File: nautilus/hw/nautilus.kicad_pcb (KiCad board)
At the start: 4 copper layers, 54.8 x 54 mm, 100 parts, among them IC1 DRV8353SRTAR, IC2 STM32G474CEU6, IC3 MAX15062AATA+T, J1 XT30XT30PW_MALE, J2 Conn_01x02_Pin, J3 Conn_01x02_Pin, U2 CSD88599Q5DCT, U3 CSD88599Q5DCT, U4 AS5147, U5 CSD88599Q5DCT

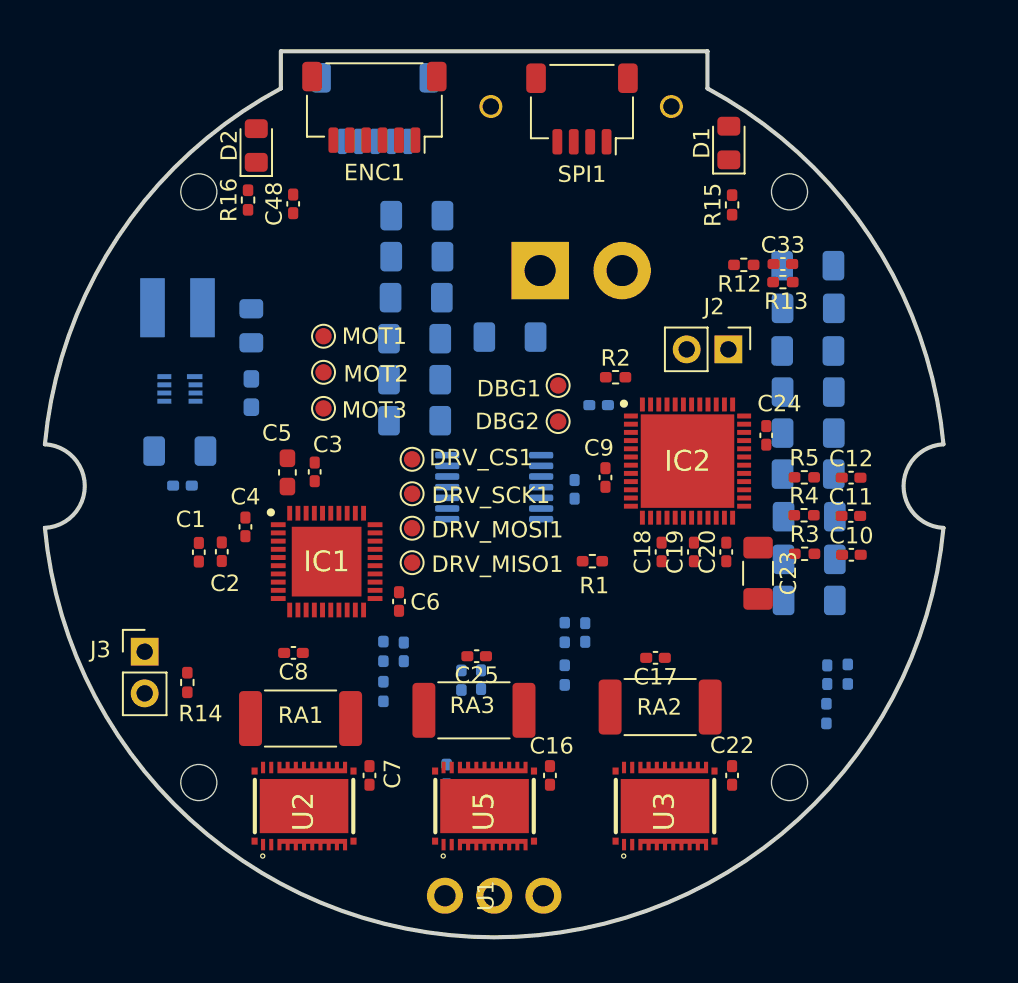
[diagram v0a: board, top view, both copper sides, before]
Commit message: First PCB layout, before DRC.
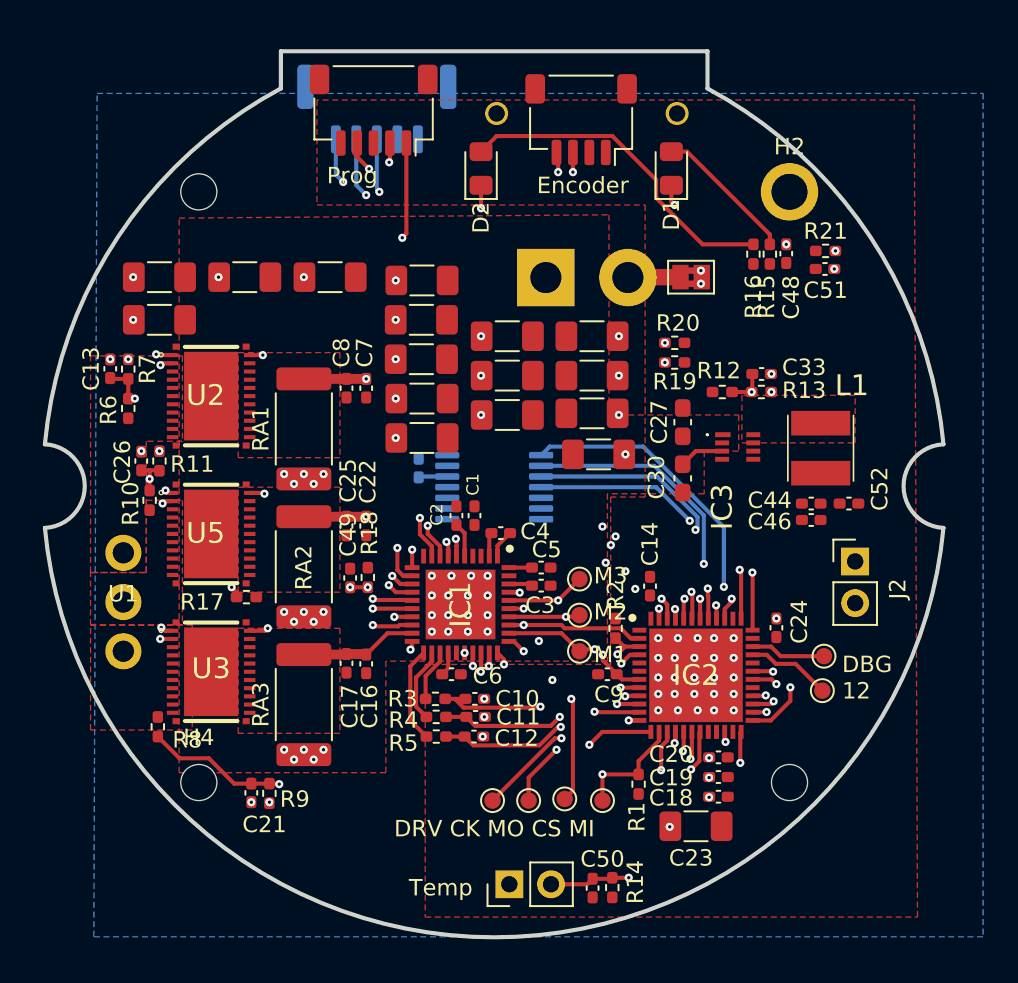
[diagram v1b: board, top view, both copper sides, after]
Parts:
- removed ENC1: PICO-SPOX-6NOPASTE, Connector_JST:JST_SH_SM06B-SRSS-TB_1x06-1MP_P1.00mm_Horizontal
- added C50: 10nF, Capacitor_SMD:C_0402_1005Metric_Pad0.74x0.62mm_HandSolder, F.Cu at (152.0, 106.8)
- added C51: 10nF, Capacitor_SMD:C_0402_1005Metric_Pad0.74x0.62mm_HandSolder, F.Cu at (166.2, 69.1)
- added C52: 0.1uF, Capacitor_SMD:C_0402_1005Metric_Pad0.74x0.62mm_HandSolder, F.Cu at (167.6, 83.4)
- added JP1: SolderJumper_2_Bridged, Jumper:SolderJumper-2_P1.3mm_Bridged2Bar_Pad1.0x1.5mm, F.Cu at (158.0, 69.6)
- added R19: 5k, Resistor_SMD:R_0402_1005Metric_Pad0.72x0.64mm_HandSolder, F.Cu at (157.0, 74.8)
- added R20: 5k, Resistor_SMD:R_0402_1005Metric_Pad0.72x0.64mm_HandSolder, F.Cu at (157.0, 73.6)
- added R21: 100k, Resistor_SMD:R_0402_1005Metric_Pad0.72x0.64mm_HandSolder, F.Cu at (166.2, 68.0)
- added SPI2: JST_SH4, Connector_JST:JST_SH_SM04B-SRSS-TB_1x04-1MP_P1.00mm_Horizontal, F.Cu at (151.3, 60.0)
- C13, C14, C21, C26, C28, C29, C30, C31, C32, C34, C35, C36, C37, C38, C39, C40, C41, C42, C43, C45, C46, C47, C49, DEBUG1, IC3, L1, R10, R11, R17, R18, R6, R7, R8, R9: moved to F.Cu
- C27: value 1uF 100V -> 1uF; footprint Capacitor_SMD:C_0805_2012Metric_Pad1.18x1.45mm_HandSolder -> Capacitor_SMD:C_0603_1608Metric_Pad1.08x0.95mm_HandSolder; moved to F.Cu
- C33: value 0.01uF -> 10nF
- C44: footprint Capacitor_SMD:C_1206_3216Metric_Pad1.33x1.80mm_HandSolder -> Capacitor_SMD:C_0402_1005Metric_Pad0.74x0.62mm_HandSolder; moved to F.Cu
- C5: footprint Capacitor_SMD:C_0603_1608Metric_Pad1.08x0.95mm_HandSolder -> Capacitor_SMD:C_0402_1005Metric_Pad0.74x0.62mm_HandSolder
- H2: footprint MountingHole:MountingHole_2.2mm_M2_ISO7380 -> MountingHole:MountingHole_2.2mm_M2_ISO7380_Pad
- R1: value 2k -> 10k
- RA1, RA2, RA3: value 0.5mOhm 1% 2W -> 1.0mOhm 1% 2W
- SPI1: value JST_ZH4 -> JST_ZH5; footprint Connector_JST:JST_SH_SM04B-SRSS-TB_1x04-1MP_P1.00mm_Horizontal -> Connector_JST:JST_GH_SM05B-GHS-TB_1x05-1MP_P1.25mm_Horizontal; moved to B.Cu
- moved R8 40.8 mm to (125.5, 97.0), turned to 90 degrees
- moved L1 40.1 mm to (165.9, 80.0), turned to 90 degrees
- moved C42 39.5 mm to (125.6, 72.2), turned to 180 degrees
- moved C43 39.5 mm to (125.6, 69.6), turned to 180 degrees
- moved C44 38.6 mm to (165.3, 83.4), turned to 180 degrees
- moved C46 38.4 mm to (165.3, 84.4), turned to 180 degrees
- moved R9 36.0 mm to (132.3, 101.1), turned to 90 degrees
- moved C21 35.8 mm to (131.2, 101.0), turned to -90 degrees
- moved C31 35.2 mm to (136.0, 69.6), turned to 180 degrees
- moved C41 34.6 mm to (130.8, 69.6), turned to 180 degrees
- moved IC3 34.2 mm to (160.8, 80.0)
- moved R16 31.0 mm to (161.8, 68.2)
- moved C48 30.2 mm to (163.8, 68.2)
- moved C26 29.0 mm to (124.5, 80.8)
- moved U3 28.8 mm to (128.8, 93.7), turned to 0 degrees
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- renumbered MOT1 to M1, MOT2 to M2, MOT3 to M3
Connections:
- net +3V3 renamed +3.3V
- C1 pad 2: GND -> GNDPWR
- C10 pad 2: GND -> GNDS
- C11 pad 2: GND -> GNDS
- C12 pad 2: GND -> GNDS
- C13 pad 2: GND -> GNDS
- C14 pad 2: GND -> GNDS
- C15 pad 2: GND -> GNDS
- C17 pad 2: GND -> GNDPWR
- C18 pad 2: GND -> GNDS
- C19 pad 2: GND -> GNDS
- C20 pad 2: GND -> GNDS
- C21 pad 2: GND -> GNDS
- C23 pad 1: GND -> GNDS
- C24 pad 2: GND -> GNDS
- C25 pad 2: GND -> GNDPWR
- C26 pad 2: GND -> GNDS
- C27 pad 2: GND -> GNDS
- C28 pad 2: GND -> GNDPWR
- C29 pad 2: GND -> GNDPWR
- C3 pad 2: GND -> GNDPWR
- C30 pad 2: GND -> GNDS
- C31 pad 2: GND -> GNDPWR
- C32 pad 2: GND -> GNDPWR
- C33 pad 2: GND -> GNDS
- C34 pad 2: GND -> GNDPWR
- C35 pad 2: GND -> GNDPWR
- C36 pad 2: GND -> GNDPWR
- C37 pad 2: GND -> GNDPWR
- C38 pad 2: GND -> GNDPWR
- C39 pad 2: GND -> GNDPWR
- C40 pad 2: GND -> GNDPWR
- C41 pad 2: GND -> GNDPWR
- C42 pad 2: GND -> GNDPWR
- C43 pad 2: GND -> GNDPWR
- C44 pad 2: GND -> GNDS
- C45 pad 2: GND -> GNDPWR
- C46 pad 2: GND -> GNDS
- C47 pad 2: GND -> GNDPWR
- C48 pad 2: GND -> GNDS
- C49 pad 2: GND -> GNDS
- C5 pad 1: GND -> Net-(IC1-VGLS)
- C5 pad 2: Net-(IC1-VGLS) -> GNDPWR
- C6 pad 1: GND -> GNDS
- C8 pad 2: GND -> GNDPWR
- C9 pad 2: GND -> GNDS
- DEBUG1 pad 3: GND -> GNDS
- IC1 pad 10: GND -> GNDPWR
- IC1 pad 11: GND -> GNDPWR
- IC1 pad 20: GND -> GNDPWR
- IC1 pad 25: GND -> GNDS
- IC1 pad 39: GND -> GNDPWR
- IC1 pad 41: GND -> GNDS
- IC2 pad 2: /SECONDARY_ENC_CS -> /MOTOR_HIZ
- IC2 pad 29: /DRV8323_CS -> unconnected-(IC2-PC6-Pad29)
- IC2 pad 3: /DEBUG1 -> /MOTOR_FAULT
- IC2 pad 32: GND -> GNDS
- IC2 pad 33: unconnected-(IC2-PA11-Pad33) -> /DEBUG2
- IC2 pad 34: unconnected-(IC2-PA12-Pad34) -> /DEBUG1
- IC2 pad 4: /DEBUG2 -> /DRV8323_CS
- IC2 pad 44: /MOTOR_FAULT -> /LED1
- IC2 pad 45: /MOTOR_HIZ -> /LED2
- IC2 pad 46: unconnected-(IC2-PB8-BOOT0-Pad46) -> /I2C_ABS_SCL
- IC2 pad 47: unconnected-(IC2-PB9-Pad47) -> /I2C_ABS_SDA
- IC2 pad 49: GND -> GNDS
- IC2 pad 5: /LED1 -> unconnected-(IC2-PF0-OSC_IN-Pad5)
- IC2 pad 6: /LED2 -> unconnected-(IC2-PF1-OSC_OUT-Pad6)
- IC3 pad 7: GND -> GNDS
- J1 pad 2: GND -> GNDPWR
- R11 pad 1: GND -> GNDS
- R13 pad 1: GND -> GNDS
- R14 pad 2: GND -> GNDS
- R18 pad 2: GND -> GNDS
- R7 pad 1: GND -> GNDS
- R9 pad 1: GND -> GNDS
- RA1 pad 1: GND -> GNDPWR
- RA2 pad 1: GND -> GNDPWR
- RA2 pad 2: /SXC_P -> /SXB_P
- RA3 pad 1: GND -> GNDPWR
- RA3 pad 2: /SXB_P -> /SXC_P
- U4 pad 13: GND -> GNDS
- U4 pad 5: GND -> GNDS
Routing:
- net /SWCLK: track 0.00 -> 45.6 mm, vias 0 -> 3
- net /SWDIO: track 0.00 -> 45.2 mm, vias 0 -> 3
- net /SPI3_SCK: track 0.00 -> 44.5 mm, vias 0 -> 3
- net /VSENSE_B: track 0.00 -> 43.5 mm, vias 0 -> 2
- net /VSENSE_A: track 0.00 -> 43.2 mm, vias 0 -> 2
- net /SPI3_MISO: track 0.00 -> 42.4 mm, vias 0 -> 3
- net /SPI3_MOSI: track 0.00 -> 40.7 mm, vias 0 -> 3
- net /NRST: track 0.00 -> 39.4 mm, vias 0 -> 2
- net /VSENSE_C: track 0.00 -> 39.1 mm, vias 0 -> 2
- net /VTEMP_FET: track 0.00 -> 37.5 mm, vias 0 -> 5
- net /LED2: track 0.00 -> 34.3 mm, vias 0 -> 3
- net /I2C_ABS_SDA: track 0.00 -> 31.5 mm, vias 0 -> 3
- net /I2C_ABS_SCL: track 0.00 -> 31.4 mm, vias 0 -> 3
- net /AS5047_MISO: track 0.00 -> 27.2 mm, vias 0 -> 2
- net /AS5047_CS: track 0.00 -> 27.1 mm, vias 0 -> 2
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- added copper zone on F.Cu, net +3.3V
- added copper zone on F.Cu, net /MOTOR_A
- added copper zone on F.Cu, net /MOTOR_B
- added copper zone on F.Cu, net /MOTOR_C
- added copper zone on F.Cu, net /SXA_P
- added copper zone on F.Cu, net /SXB_P
- added copper zone on F.Cu, net /SXC_P
- added copper zone on F.Cu, net /VSW
- added copper zone on In1.Cu, net GNDPWR
- added copper zone on B.Cu, net GNDS
- added copper zone on F.Cu, net V+
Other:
- board text added: "DBG 12"
- board text added: "DRV CK MO CS MI"
- board text added: "Encoder"
- board text added: "Prog"
- board text added: "SPI"
- board text added: "Temp"

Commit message: First PCB design passing DRC
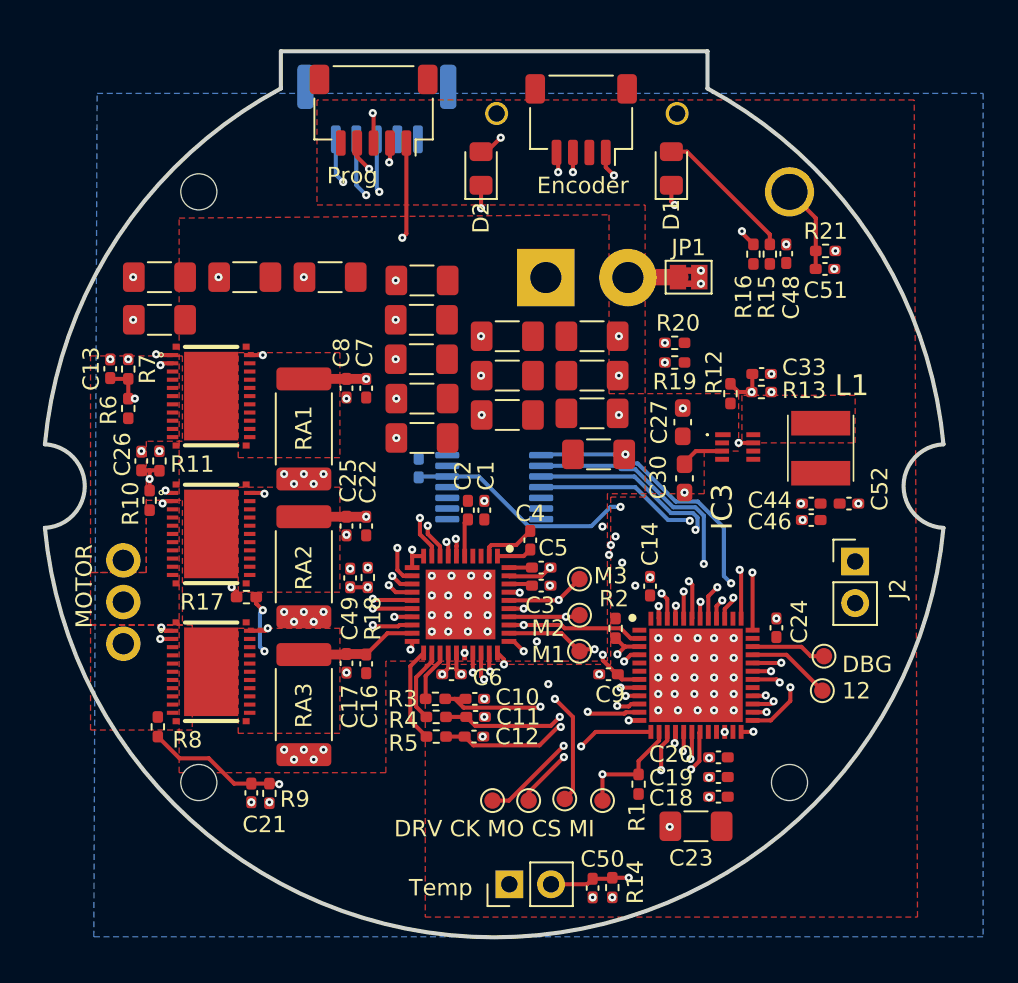
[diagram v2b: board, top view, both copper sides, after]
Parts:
- H2: footprint MountingHole:MountingHole_2.2mm_M2_ISO7380_Pad -> nautilus:MountingHole-Plated
- moved C4 1.85 mm to (148.2, 85.6), turned to 90 degrees
- moved C2 0.77 mm to (144.4, 83.8)
- moved C1 0.69 mm to (145.4, 83.8)
- moved R12 0.51 mm to (160.4, 76.7), turned to -90 degrees
- moved JP1 0.15 mm to (157.8, 69.6)
- moved C30 0.11 mm to (157.6, 81.9)
- moved C9 0.07 mm to (153.0, 93.8)
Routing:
- net +3.3V: track 3.21 -> 30.6 mm, vias 0 -> 4
- net GNDS: track 0.00 -> 7.51 mm, vias 60 -> 76
- net Net-(C51-Pad1): track 0.00 -> 5.36 mm
- net GNDPWR: track 4.85 -> 8.28 mm, vias 35 -> 41
- net Net-(IC1-CPH): track 1.45 -> 3.46 mm
- net /LED1: track 26.8 -> 27.4 mm
- net Net-(D2-A): track 20.4 -> 19.7 mm, vias 0 -> 2
- net /AS5047_CS: track 27.1 -> 26.6 mm
- net /MOTOR3: track 14.1 -> 14.6 mm
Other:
- board text added: "MOTOR"

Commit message: Cleanup PCB before order
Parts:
- removed JP1: SolderJumper_2_Bridged, Jumper:SolderJumper-2_P1.3mm_Bridged2Bar_Pad1.0x1.5mm
- added C53: 10uF 50V, Capacitor_SMD:C_1206_3216Metric_Pad1.33x1.80mm_HandSolder, F.Cu at (160.7, 72.5)
- added C54: 10uF, Capacitor_SMD:C_1206_3216Metric_Pad1.33x1.80mm_HandSolder, F.Cu at (130.8, 71.2)
- added C55: 10uF, Capacitor_SMD:C_1206_3216Metric_Pad1.33x1.80mm_HandSolder, F.Cu at (136.0, 72.2)
- added C56: 10uF, Capacitor_SMD:C_1206_3216Metric_Pad1.33x1.80mm_HandSolder, F.Cu at (141.7, 67.2)
- added C57: 10uF, Capacitor_SMD:C_1206_3216Metric_Pad1.33x1.80mm_HandSolder, F.Cu at (136.0, 67.2)
- added D3: D_Schottky, Diode_SMD:D_SOD-123F, F.Cu at (156.6, 78.0)
- added D4: D_Schottky, Diode_SMD:D_SOD-123F, F.Cu at (156.7, 73.3)
- added J4: Conn_01x02_Pin, Connector_Molex:Molex_PicoBlade_53047-0210_1x02_P1.25mm_Vertical, F.Cu at (145.7, 61.0)
- added NT1: NetTie_2, NetTie:NetTie-2_SMD_Pad0.5mm, F.Cu at (136.9, 97.7)
- added NT2: NetTie_2, NetTie:NetTie-2_SMD_Pad0.5mm, F.Cu at (136.9, 80.3)
- added NT3: NetTie_2, NetTie:NetTie-2_SMD_Pad0.5mm, F.Cu at (135.7, 88.5)
- added NT4: NetTie_2, NetTie:NetTie-2_SMD_Pad0.5mm, F.Cu at (152.8, 66.2)
- added U7: SN65HVD232, Package_SO:SOIC-8_3.9x4.9mm_P1.27mm, B.Cu at (162.4, 71.9)
- C23: value 10uF -> 10uF 50V
- C28, C29, C31, C32, C34, C35, C36, C37, C38, C39, C40, C41, C42, C43, C45, C47: value 10uF 50V -> 10uF
- C44: value 10uF -> 10uF 50V; footprint Capacitor_SMD:C_0402_1005Metric_Pad0.74x0.62mm_HandSolder -> Capacitor_SMD:C_1206_3216Metric_Pad1.33x1.80mm_HandSolder
- C49: value 0.1uF -> 10nF
- H1, H3, H4: footprint MountingHole:MountingHole_2.2mm_M2_ISO7380 -> nautilus:MountingHole-Plated
- R10, R6, R8: value 100k -> 100k 1%
- R11, R7, R9: value 5.1k -> 4.7k 1%
- RA1, RA2, RA3: value 1.0mOhm 1% 2W -> 0.5mOhm 1% 2W
- moved D1 12.5 mm to (146.3, 56.2), turned to 0 degrees
- moved C33 6.50 mm to (160.3, 81.7)
- moved R13 6.50 mm to (160.3, 82.8)
- moved R12 6.42 mm to (157.7, 82.5), turned to 180 degrees
- moved D2 5.94 mm to (143.3, 57.4), turned to -90 degrees
- moved R20 5.91 mm to (158.9, 68.0)
- moved R19 5.77 mm to (158.9, 69.3)
- moved R2 5.02 mm to (157.5, 88.1)
- moved L1 3.33 mm to (167.7, 77.2)
- moved C27 3.33 mm to (159.3, 75.6)
- moved C30 3.33 mm to (159.4, 79.1)
- moved IC3 3.33 mm to (162.7, 77.2)
- moved C52 3.18 mm to (164.5, 83.0)
- moved C21 2.34 mm to (131.2, 103.4)
- moved R9 2.34 mm to (132.3, 103.4)
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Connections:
- net /FCUR1 renamed Net-(IC2-PB0)
- net /FCUR2 renamed Net-(IC2-PB1)
- net /FCUR3 renamed Net-(IC2-PB2)
- C17 pad 2: GNDPWR -> /SXC_N
- C23 pad 1: GNDS -> +3.3V
- C23 pad 2: +3.3V -> GNDS
- C25 pad 2: GNDPWR -> /SXB_N
- C27 pad 1: V+ -> Net-(D3-K)
- C8 pad 2: GNDPWR -> /SXA_N
- DEBUG1 pad 5: +3.3V -> +5V
- IC1 pad 10: GNDPWR -> /SXA_N
- IC1 pad 11: GNDPWR -> /SXB_N
- IC1 pad 20: GNDPWR -> /SXC_N
- IC2 pad 2: /MOTOR_HIZ -> /DRV8323_CS
- IC2 pad 3: /MOTOR_FAULT -> /DEBUG1
- IC2 pad 33: /DEBUG2 -> /CAN_RX
- IC2 pad 34: /DEBUG1 -> /CAN_TX
- IC2 pad 4: /DRV8323_CS -> /DEBUG2
- IC2 pad 44: /LED1 -> /MOTOR_FAULT
- IC2 pad 45: /LED2 -> /MOTOR_HIZ
- IC2 pad 5: unconnected-(IC2-PF0-OSC_IN-Pad5) -> /LED1
- IC2 pad 6: unconnected-(IC2-PF1-OSC_OUT-Pad6) -> /LED2
- IC3 pad 1: V+ -> Net-(D3-K)
- IC3 pad 2: V+ -> Net-(D3-K)
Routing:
- net +5V: track 0.00 -> 30.3 mm
- net /CAN_TX: track 0.00 -> 22.1 mm, vias 0 -> 2
- net /LED1: track 27.4 -> 49.4 mm
- net Net-(J4-Pin_1): track 0.00 -> 21.1 mm, vias 0 -> 1
- net /CAN_RX: track 0.00 -> 21.0 mm, vias 0 -> 2
- net Net-(J4-Pin_2): track 0.00 -> 20.8 mm, vias 0 -> 1
- net Net-(D1-A): track 8.69 -> 20.1 mm, vias 0 -> 2
- net /LED2: track 34.0 -> 44.7 mm, vias 3 -> 2
- net /SXA_N: track 0.00 -> 9.62 mm, vias 0 -> 2
- net /DEBUG2: track 5.16 -> 14.6 mm, vias 0 -> 2
- net /SXC_N: track 0.00 -> 7.88 mm, vias 0 -> 2
- net /DEBUG1: track 4.59 -> 12.3 mm, vias 0 -> 2
- net /SXB_N: track 0.00 -> 6.76 mm, vias 0 -> 2
- net /SXA_P: track 16.3 -> 10.9 mm
- net /VBAT_SENSE: track 25.2 -> 21.5 mm
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- added copper zone on F.Cu, net Net-(D3-K)
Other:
- board size 54.8 x 54 mm -> 54.7 x 55 mm
- board text added: "CAN"
- board text added: "CK MO CS MI"
- board text removed: "DRV CK MO CS MI"

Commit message: Minor PCB update
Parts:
- added SW1: SW_Push, Button_Switch_SMD:SW_SPST_B3U-1000P, F.Cu at (139.6, 69.3)
- moved C43 23.9 mm to (146.8, 80.4), turned to 180 degrees
- moved C56 2.55 mm to (144.0, 68.3)
- moved C38 2.53 mm to (144.0, 70.7)
- moved C31 1.95 mm to (134.2, 68.9), turned to 90 degrees
- moved C57 1.85 mm to (136.6, 69.0), turned to 90 degrees
- moved C28 1.00 mm to (141.7, 75.6)
- moved C34 1.00 mm to (141.7, 73.2)
- moved C35 1.00 mm to (141.7, 80.4)
- moved C47 1.00 mm to (141.7, 78.0)
- moved C30 0.83 mm to (160.2, 79.0), turned to 90 degrees
- moved C55 0.75 mm to (135.4, 72.7)
- moved C41 0.55 mm to (130.3, 69.0)
- moved C54 0.54 mm to (130.3, 71.4)
- moved C42 0.47 mm to (125.2, 72.1)
- moved NT4 0.15 mm to (152.8, 66.3)
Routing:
- net GNDS: track 7.23 -> 9.13 mm, vias 76 -> 79
- net /NRST: track 41.1 -> 42.6 mm, vias 2 -> 3
- net /SWDIO: track 45.5 -> 45.0 mm
- added copper zone on In2.Cu, net GNDS

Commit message: [Hardware] First prototype order
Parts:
- C27, C30: footprint Capacitor_SMD:C_0603_1608Metric_Pad1.08x0.95mm_HandSolder -> Capacitor_SMD:C_0402_1005Metric_Pad0.74x0.62mm_HandSolder
- moved C30 0.87 mm to (159.4, 79.2), turned to -90 degrees
- moved C27 0.40 mm to (158.9, 75.6)

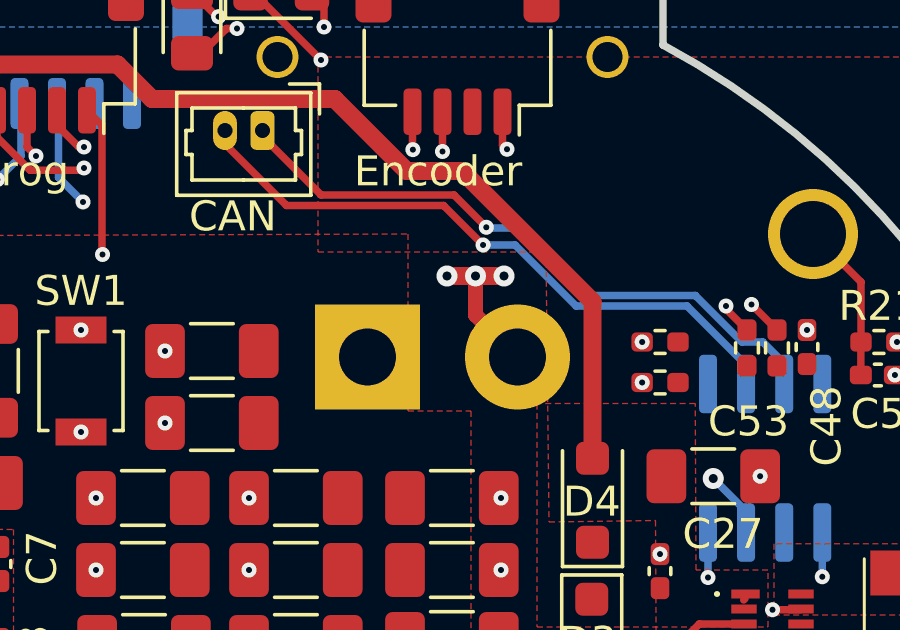
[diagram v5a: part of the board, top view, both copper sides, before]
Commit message: First prototype assembly
 - [hw] Fix reverse XT-30 connector in PCB
 - [sw] Add led blink to SPI communication
 - [sw] Add note about using SPI1 mode only (other modes don't work)
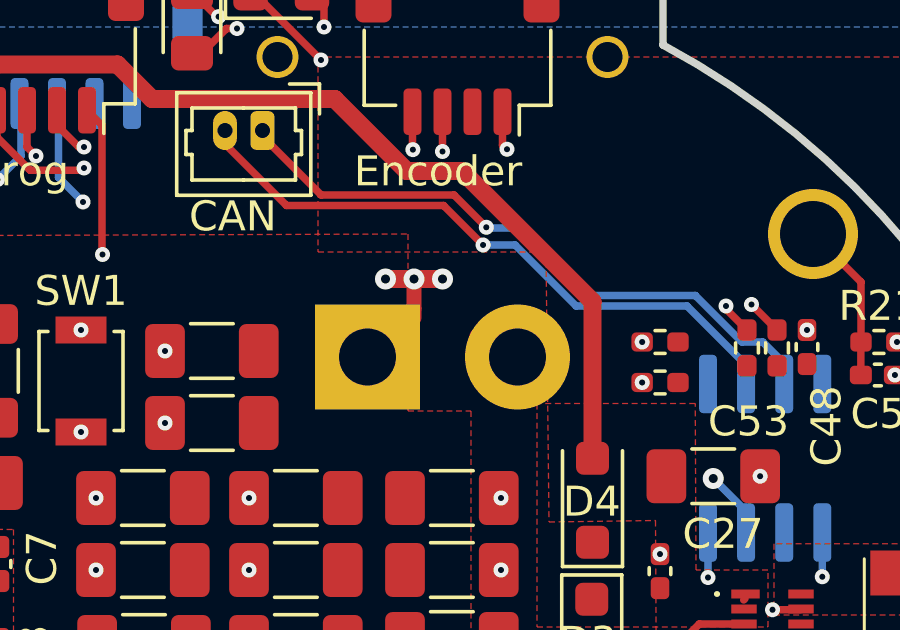
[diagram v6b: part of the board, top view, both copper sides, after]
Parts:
- moved NT4 2.05 mm to (150.7, 66.4)
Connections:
- IC2 pad 38: unconnected-(IC2-PA15-Pad38) -> /SPI3_CS
- J1 pad 1: V+ -> GNDPWR
- J1 pad 2: GNDPWR -> V+
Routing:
- net GNDPWR: track 10.6 -> 8.15 mm
